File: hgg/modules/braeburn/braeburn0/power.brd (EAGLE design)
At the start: 104.4 x 72.9 mm, 69 parts, among them IC1 LM324D, IC4 ATMEGA48/88/168-AU, IC5 LTC485S, Q1 20Mhz

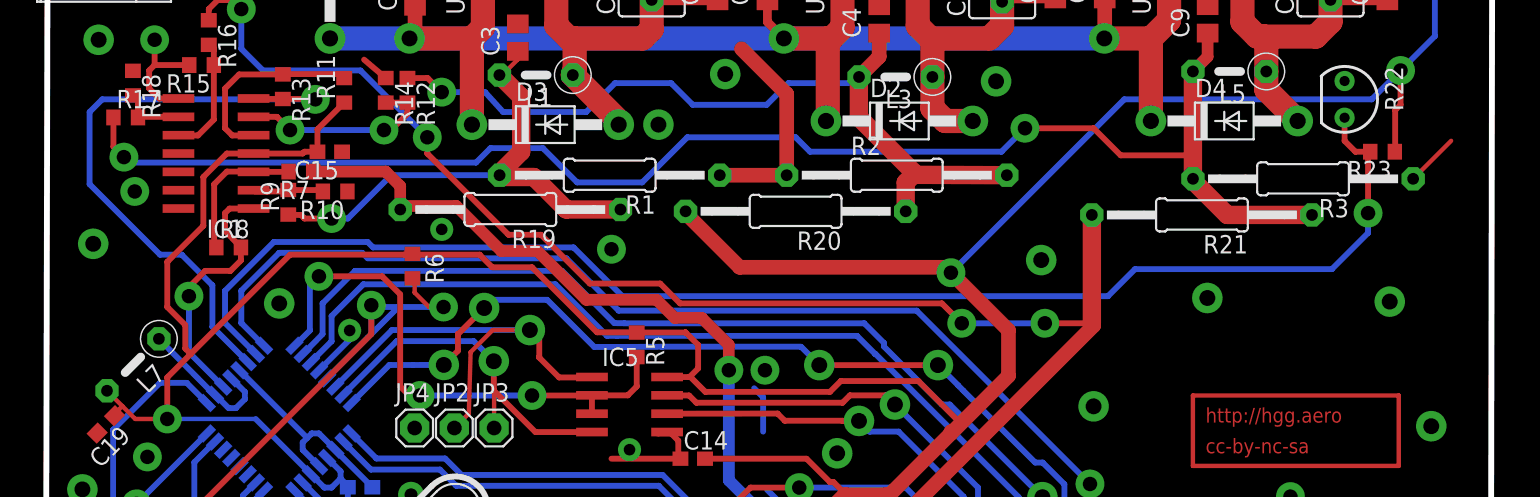
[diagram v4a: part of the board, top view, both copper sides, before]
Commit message: less thrughhole parts
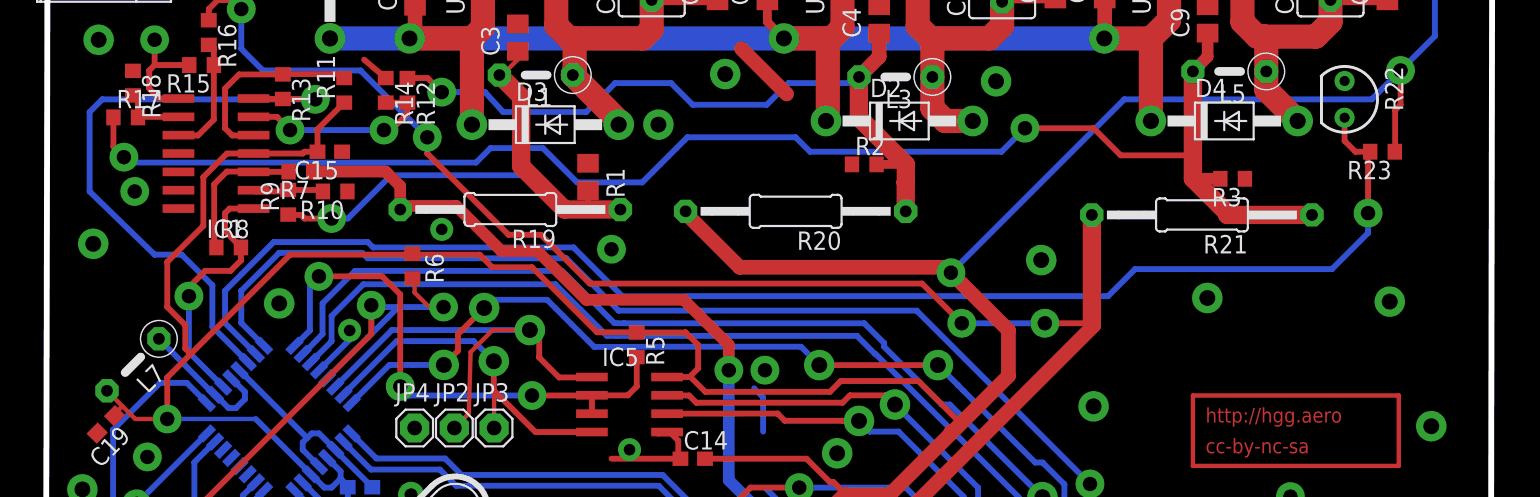
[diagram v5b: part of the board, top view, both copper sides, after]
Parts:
- R1: device rcl:0207/15 -> rcl:R0805
- R2, R3: device rcl:0207/15 -> rcl:R0603
- moved R3 4.88 mm to (83.6, 36.9)
- moved R2 2.37 mm to (58.1, 37.9)
- moved R1 1.51 mm to (39.0, 37.0), turned to 270 degrees
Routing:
- net GND: track 253.4 -> 239.5 mm
- net 3V3IN: track 35.8 -> 45.5 mm
- net VCCIN: track 55.7 -> 50.8 mm
- net 12VIN: track 101.7 -> 103.6 mm
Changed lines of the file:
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@@
 <element name="L5" library="resistor" package="0207/5V" value="33u" x="83.415" y="44.307" rot="R180"/>
 <element name="C13" library="resistor" package="C025-060X050" value="2000u" x="14.688" y="55.483" rot="R270"/>
-<element name="R1" library="rcl" package="0207/15" value="330" x="40.5" y="37.125" rot="R180"/>
-<element name="R2" library="rcl" package="0207/15" value="500" x="60.375" y="37.125"/>
-<element name="R3" library="rcl" package="0207/15" value="1k2" x="88.5" y="36.875" rot="R180"/>
+<element name="R1" library="rcl" package="R0805" value="330" x="39" y="37" rot="R270"/>
+<element name="R2" library="rcl" package="R0603" value="500" x="58.125" y="37.875"/>
+<element name="R3" library="rcl" package="R0603" value="1k2" x="83.625" y="36.875" rot="R180"/>
 <element name="D1" library="diode" package="DO41-10" value="1N4004" x="21.141" y="51.673" rot="R90"/>
 <element name="D2" library="diode" package="DO41-10" value="1N4004" x="60.555" y="40.878"/>
@@
 <wire x1="21.51285625" y1="18.1172" x2="21.51285625" y2="18.08214375" width="0.4064" layer="16"/>
 <wire x1="21.51285625" y1="18.08214375" x2="24.07" y2="15.525" width="0.4064" layer="16"/>
-<wire x1="48.12" y1="37.125" x2="52.755" y2="37.125" width="1.016" layer="1"/>
-<wire x1="52.755" y1="37.125" x2="52.755" y2="42.745" width="1.016" layer="1"/>
 <wire x1="52.755" y1="42.745" x2="49.625" y2="45.875" width="1.016" layer="1"/>
 <contactref element="C14" pad="1"/>
@@
 <wire x1="5.625" y1="51.353" x2="5.945" y2="51.673" width="1.016" layer="16"/>
 <wire x1="94.337" y1="51.099" x2="94.337" y2="51.462" width="0.3048" layer="1"/>
-<wire x1="98.75" y1="39.505" x2="96.12" y2="36.875" width="0.3048" layer="1"/>
 <polygon width="0.254" layer="1" isolate="0.6096">
 <vertex x="-37.875" y="-11"/>
@@
 <wire x1="33.5" y1="33" x2="35.75" y2="33" width="0.4064" layer="1"/>
 <wire x1="35.75" y1="33" x2="39.125" y2="29.625" width="0.4064" layer="1"/>
-<wire x1="39.125" y1="29.625" x2="44" y2="29.625" width="0.4064" layer="1"/>
-<wire x1="44" y1="29.625" x2="45.375" y2="28.25" width="0.4064" layer="1"/>
-<wire x1="45.375" y1="28.25" x2="63.5" y2="28.25" width="0.4064" layer="1"/>
-<wire x1="63.5" y1="28.25" x2="64.875" y2="26.875" width="0.4064" layer="1"/>
+<wire x1="39.125" y1="29.625" x2="62.125" y2="29.625" width="0.4064" layer="1"/>
+<wire x1="62.125" y1="29.625" x2="64.875" y2="26.875" width="0.4064" layer="1"/>
 <via x="64.875" y="26.875" extent="1-16" drill="1" shape="octagon"/>
 <wire x1="64.875" y1="26.875" x2="70.625" y2="26.875" width="0.4064" layer="16"/>
@@
 <wire x1="38.515" y1="21.875" x2="35.125" y2="21.875" width="0.4064" layer="1"/>
 <via x="35.125" y="21.875" extent="1-16" drill="1" shape="octagon"/>
-<wire x1="35.125" y1="21.875" x2="27.375" y2="21.875" width="0.4064" layer="16"/>
-<via x="27.375" y="21.875" extent="1-16" drill="1" shape="octagon"/>
-<wire x1="27.375" y1="21.875" x2="26.625" y2="21.875" width="0.4064" layer="1"/>
+<wire x1="35.125" y1="21.875" x2="26.625" y2="21.875" width="0.4064" layer="16"/>
 <wire x1="24.75" y1="30.125" x2="20.375" y2="30.125" width="0.4064" layer="1"/>
 <via x="20.375" y="30.125" extent="1-16" drill="1" shape="octagon"/>
@@
 <wire x1="24.75" y1="30.125" x2="26" y2="28.875" width="0.4064" layer="1"/>
 <wire x1="26" y1="28.875" x2="26" y2="22.5" width="0.4064" layer="1"/>
-<wire x1="26" y1="22.5" x2="26.625" y2="21.875" width="0.4064" layer="1"/>
+<wire x1="26" y1="22.5" x2="26.625" y2="21.875" width="0.4064" layer="16"/>
 <wire x1="42.376" y1="24.534" x2="42.376" y2="22.501" width="0.4064" layer="1"/>
 <wire x1="39.275" y1="21.885" x2="41.76" y2="21.885" width="0.4064" layer="1"/>
 <wire x1="41.76" y1="21.885" x2="42.376" y2="22.501" width="0.4064" layer="1"/>
+<via x="26" y="22.5" extent="1-16" drill="1" shape="octagon"/>
 </signal>
 <signal name="N$23">
@@
 <via x="48.75" y="23.625" extent="1-16" drill="1" shape="octagon"/>
 <wire x1="48.75" y1="23.625" x2="48.75" y2="25.375" width="0.8128" layer="1"/>
-<wire x1="48.75" y1="25.375" x2="46.875" y2="27.25" width="0.8128" layer="1"/>
-<wire x1="46.875" y1="27.25" x2="45" y2="27.25" width="0.8128" layer="1"/>
-<wire x1="45" y1="27.25" x2="43.75" y2="28.5" width="0.8128" layer="1"/>
-<wire x1="43.75" y1="28.5" x2="38.875" y2="28.5" width="0.8128" layer="1"/>
+<wire x1="48.75" y1="25.375" x2="45.625" y2="28.5" width="0.8128" layer="1"/>
+<wire x1="45.625" y1="28.5" x2="38.875" y2="28.5" width="0.8128" layer="1"/>
 <wire x1="38.875" y1="28.5" x2="35.5" y2="31.875" width="0.8128" layer="1"/>
 <wire x1="35.5" y1="31.875" x2="33" y2="31.875" width="0.8128" layer="1"/>
@@
 <wire x1="13" y1="26.63005625" x2="13" y2="29.5" width="0.4064" layer="16"/>
 <wire x1="13" y1="29.5" x2="10.875" y2="31.625" width="0.4064" layer="16"/>
-<wire x1="10.875" y1="31.625" x2="9.375" y2="31.625" width="0.4064" layer="16"/>
-<wire x1="9.375" y1="31.625" x2="4.5" y2="36.5" width="0.4064" layer="16"/>
-<wire x1="4.5" y1="36.5" x2="4.5" y2="41.5" width="0.4064" layer="16"/>
+<wire x1="10.875" y1="31.625" x2="9" y2="31.625" width="0.4064" layer="16"/>
+<wire x1="9" y1="31.625" x2="4.5" y2="36" width="0.4064" layer="16"/>
+<wire x1="4.5" y1="36" x2="4.5" y2="41.5" width="0.4064" layer="16"/>
 <wire x1="4.5" y1="41.5" x2="5.375" y2="42.375" width="0.4064" layer="16"/>
 <wire x1="5.375" y1="42.375" x2="20.125" y2="42.375" width="0.4064" layer="16"/>
@@
 <contactref element="L1" pad="2"/>
 <contactref element="C3" pad="1"/>
-<wire x1="32.88" y1="37.125" x2="32.88" y2="37.255" width="1.016" layer="1"/>
-<wire x1="32.88" y1="37.255" x2="34.375" y2="38.75" width="1.27" layer="1"/>
-<wire x1="34.375" y1="38.75" x2="34.375" y2="42.551" width="1.27" layer="1"/>
+<wire x1="34.375" y1="37.75" x2="34.375" y2="42.551" width="1.27" layer="1"/>
 <wire x1="34.375" y1="42.551" x2="32.869" y2="44.057" width="1.27" layer="1"/>
 <contactref element="R19" pad="1"/>
-<wire x1="41.245" y1="34.75" x2="37.5" y2="34.75" width="1.27" layer="1"/>
-<wire x1="37.5" y1="34.75" x2="35.25" y2="37" width="1.27" layer="1"/>
-<wire x1="35.25" y1="37" x2="33.005" y2="37" width="1.27" layer="1"/>
-<wire x1="33.005" y1="37" x2="32.88" y2="37.125" width="0.8128" layer="1"/>
+<wire x1="37.375" y1="34.75" x2="34.375" y2="37.75" width="1.27" layer="1"/>
 <contactref element="R9" pad="1"/>
 <wire x1="21.25" y1="34.125" x2="22.375" y2="34.125" width="0.4064" layer="16"/>
 <wire x1="22.375" y1="34.125" x2="25.375" y2="37.125" width="0.4064" layer="16"/>
-<wire x1="25.375" y1="37.125" x2="32.88" y2="37.125" width="0.4064" layer="16"/>
 <via x="21.25" y="34.125" extent="1-16" drill="1" shape="octagon"/>
 <wire x1="21.25" y1="34.125" x2="19.375" y2="34.125" width="0.4064" layer="1"/>
@@
 <wire x1="34.125" y1="45.125" x2="34.125" y2="45.556" width="0.3048" layer="1"/>
 <wire x1="34.125" y1="45.556" x2="34.143" y2="45.699" width="0.3048" layer="1"/>
+<wire x1="25.375" y1="37.125" x2="35" y2="37.125" width="0.4064" layer="16"/>
+<wire x1="37.375" y1="34.75" x2="41.245" y2="34.75" width="1.27" layer="1"/>
+<wire x1="39" y1="36.05" x2="39" y2="34.875" width="0.4064" layer="1"/>
+<wire x1="37.375" y1="34.75" x2="37.5" y2="34.875" width="0.4064" layer="1"/>
+<wire x1="37.5" y1="34.875" x2="39" y2="34.875" width="0.4064" layer="1"/>
+<wire x1="35" y1="37.125" x2="37.375" y2="34.75" width="0.4064" layer="16"/>
+<wire x1="37.375" y1="34.75" x2="41.245" y2="34.75" width="0.4064" layer="16"/>
 </signal>
 <signal name="VCCIN">
@@
 <wire x1="57.761" y1="43.926" x2="59.158" y2="45.323" width="1.016" layer="1"/>
 <wire x1="59.158" y1="45.323" x2="59.158" y2="46.959" width="1.016" layer="1"/>
-<wire x1="67.995" y1="37.125" x2="61.725" y2="37.15" width="1.27" layer="1"/>
-<wire x1="61.725" y1="37.15" x2="61.625" y2="37.25" width="1.016" layer="1"/>
-<wire x1="61.625" y1="37.25" x2="57.75" y2="41.125" width="1.27" layer="1"/>
 <wire x1="57.75" y1="41.125" x2="57.75" y2="43.915" width="1.27" layer="1"/>
 <wire x1="57.75" y1="43.915" x2="57.761" y2="43.926" width="1.016" layer="1"/>
 <contactref element="R20" pad="1"/>
 <wire x1="60.995" y1="34.625" x2="60.995" y2="36.62" width="1.27" layer="1"/>
-<wire x1="60.995" y1="36.62" x2="61.625" y2="37.25" width="1.27" layer="1"/>
 <contactref element="R12" pad="1"/>
 <wire x1="26.5" y1="43.85" x2="27.9" y2="43.85" width="0.4064" layer="1"/>
@@
 <wire x1="52.875" y1="43.5" x2="57.335" y2="43.5" width="0.4064" layer="16"/>
 <wire x1="57.335" y1="43.5" x2="57.761" y2="43.926" width="0.4064" layer="16"/>
+<wire x1="60.995" y1="36.62" x2="61" y2="36.625" width="1.27" layer="1"/>
+<wire x1="61" y1="36.625" x2="61" y2="37.875" width="1.27" layer="1"/>
+<wire x1="61" y1="37.875" x2="57.75" y2="41.125" width="1.27" layer="1"/>
+<wire x1="58.975" y1="37.875" x2="61" y2="37.875" width="0.6096" layer="1"/>
 </signal>
 <signal name="12VIN">
@@
 <wire x1="80.875" y1="44.307" x2="80.875" y2="38.625" width="1.27" layer="1"/>
 <wire x1="80.875" y1="38.625" x2="80.875" y2="36.88" width="1.27" layer="1"/>
-<wire x1="80.875" y1="36.88" x2="80.88" y2="36.875" width="0.8128" layer="1"/>
+<wire x1="80.875" y1="36.88" x2="82.775" y2="36.875" width="0.8128" layer="1"/>
 <wire x1="89.12" y1="34.375" x2="83.25" y2="34.375" width="1.27" layer="1"/>
-<wire x1="83.25" y1="34.375" x2="80.75" y2="36.875" width="1.27" layer="1"/>
 <contactref element="R17" pad="1"/>
 <wire x1="6.15" y1="41.125" x2="6.15" y2="39.1" width="0.4064" layer="1"/>
@@
 <wire x1="75.875" y1="38.5" x2="80.75" y2="38.5" width="0.4064" layer="1"/>
 <wire x1="80.75" y1="38.5" x2="80.875" y2="38.625" width="0.4064" layer="1"/>
-<wire x1="80.875" y1="36.88" x2="80.75" y2="36.875" width="0" layer="19" extent="1-1"/>
+<wire x1="83.25" y1="34.375" x2="83.25" y2="34.505" width="1.27" layer="1"/>
+<wire x1="83.25" y1="34.505" x2="80.875" y2="36.88" width="1.27" layer="1"/>
 </signal>
 <signal name="TEMP1">

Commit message: .
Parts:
- C13: device resistor:C025-060X050 -> resistor:C050-055X075
- moved C13 0.28 mm to (14.9, 55.6)
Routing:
- net GND: track 239.5 -> 138.6 mm, vias 54 -> 55
- net N$12: track 15.2 -> 16.3 mm
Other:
- board size 104.4 x 72.9 mm -> 104.4 x 75 mm

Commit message: .
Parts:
- moved D1 2.47 mm to (23.3, 52.9)
- moved C13 1.87 mm to (16.8, 55.6)
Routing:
- net GND: track 138.6 -> 153.0 mm, vias 55 -> 57
- net VCC: track 271.5 -> 269.3 mm
- net N$1: track 100.0 -> 97.8 mm
- net N$12: track 16.3 -> 17.9 mm
